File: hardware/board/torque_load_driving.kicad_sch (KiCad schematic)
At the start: 22 parts, among them J4 Conn_01x02_Female, Q1 IRF8707TRPBF, U1 ADS7049, U10 AD8615, U11 INA180A4, U12 UCC27537

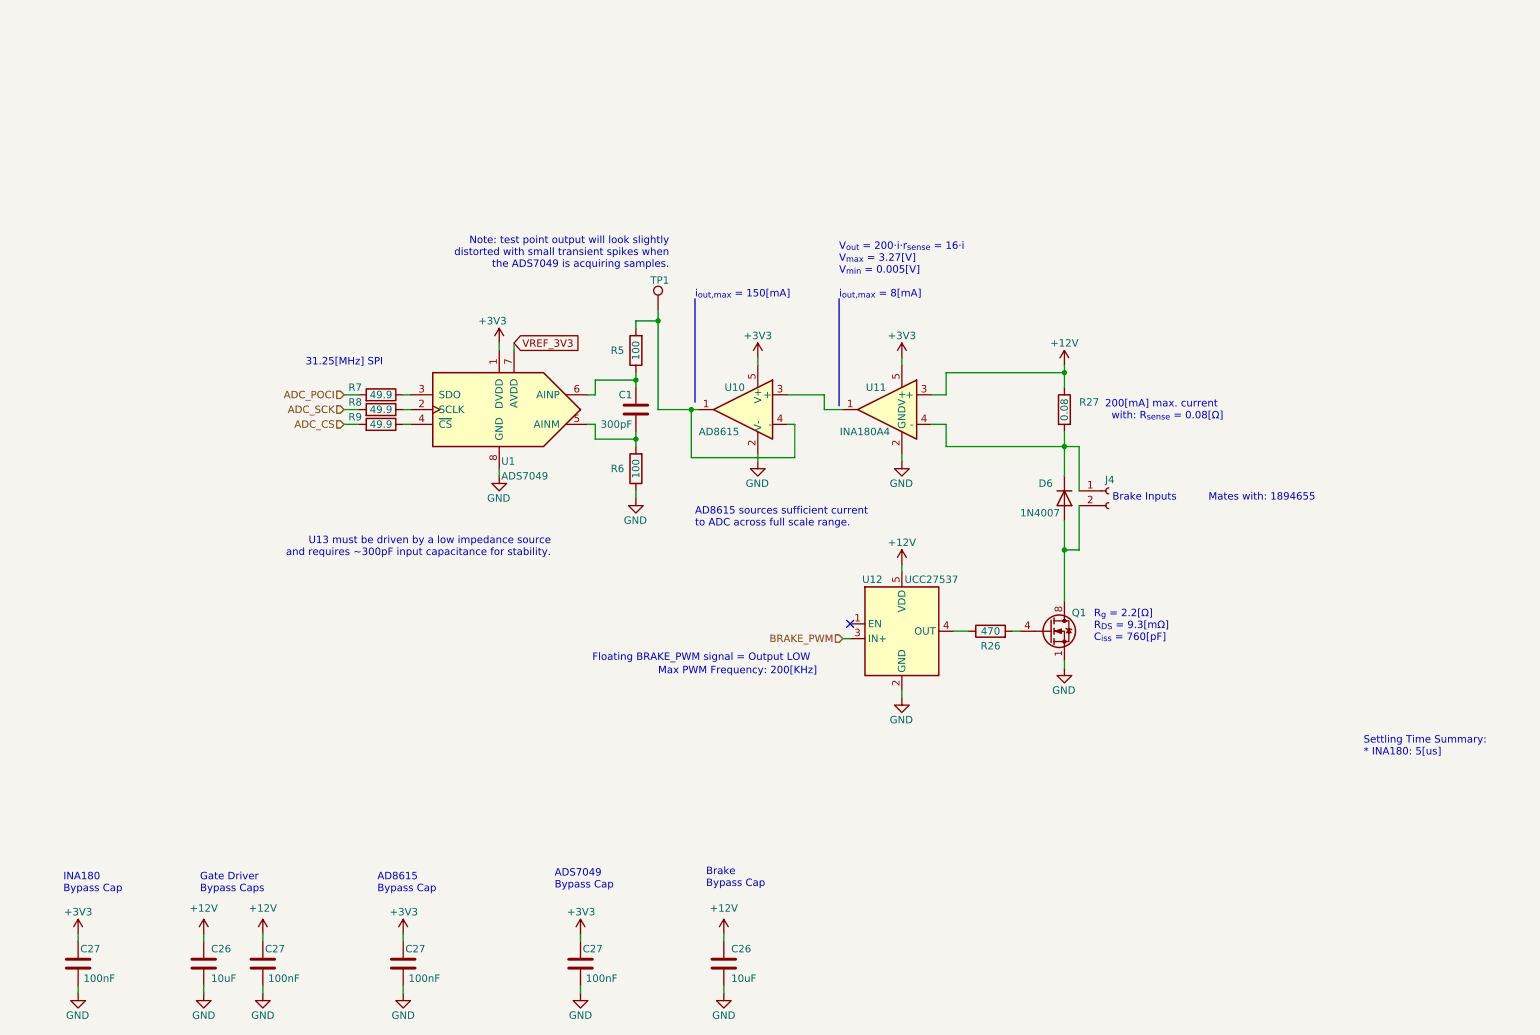
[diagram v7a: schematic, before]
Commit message: draft layout with analog brake driver circuit
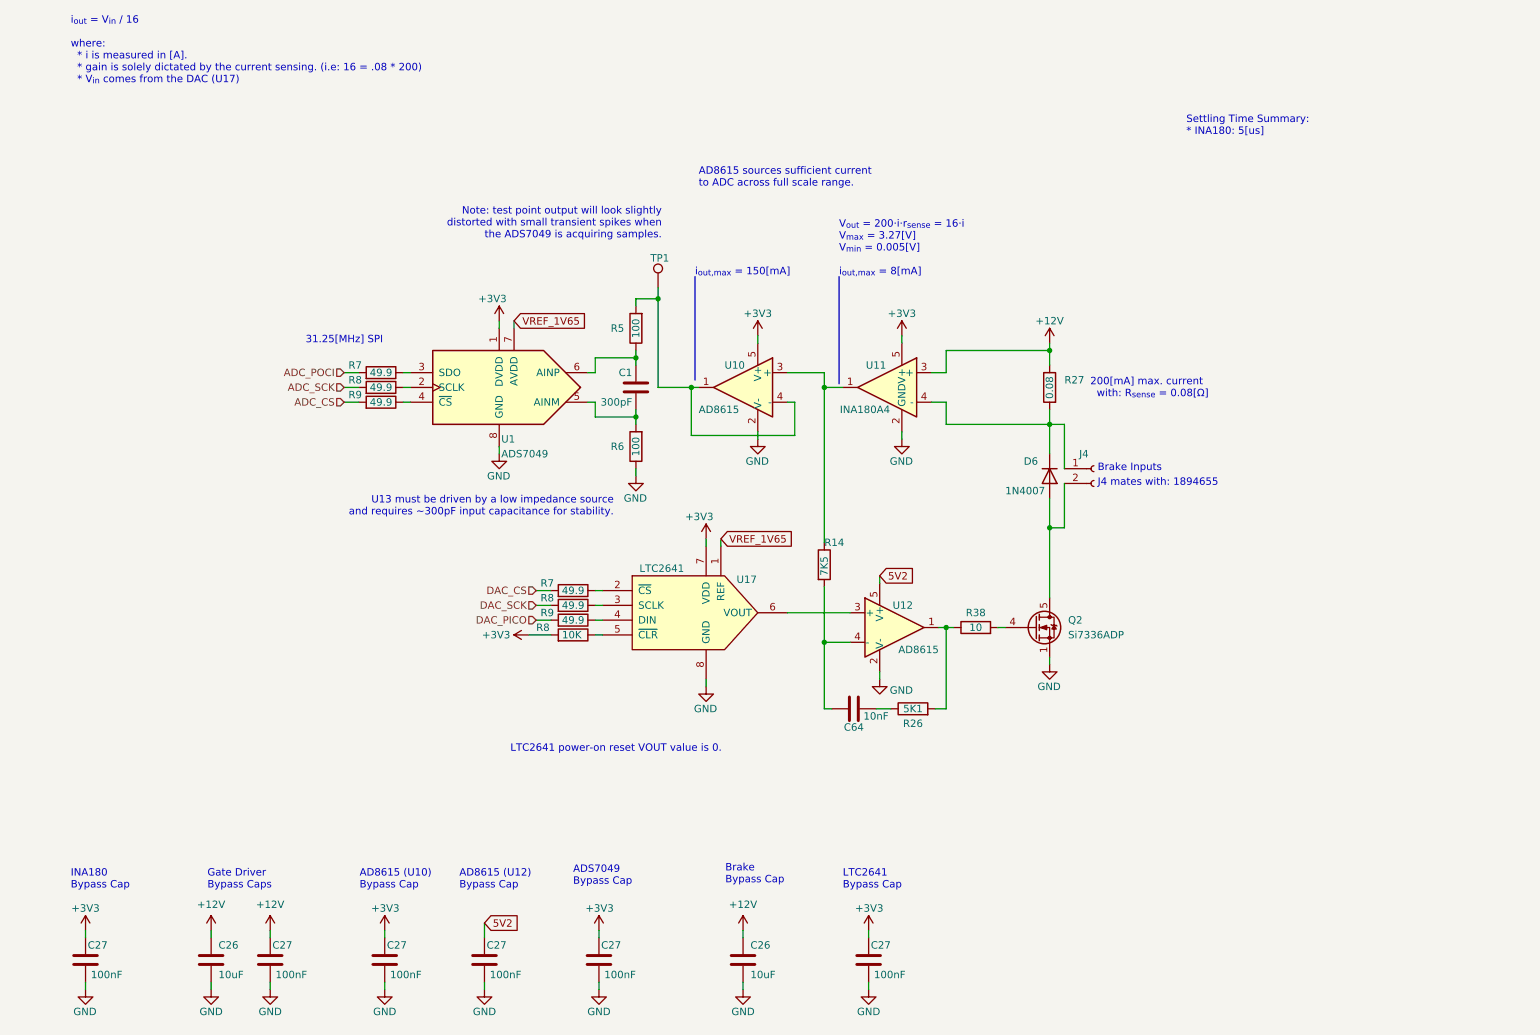
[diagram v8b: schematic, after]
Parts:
- removed Q1: IRF8707TRPBF, Package_SO:SOIC-8_3.9x4.9mm_P1.27mm, symbol Transistor_FET:IRF7403
- removed U12: UCC27537, Package_TO_SOT_SMD:SOT-23-5, symbol kicad_component_library:UCC27537
- added C27 (x2): 100nF, Capacitor_SMD:C_0402_1005Metric, symbol Device:C
- added C64: 10nF, Capacitor_SMD:C_0603_1608Metric, symbol Device:C
- added Q2: Si7336ADP, Package_SO:PowerPAK_SO-8_Single, symbol Transistor_FET:Si7336ADP
- added R14: 7K5, Resistor_SMD:R_0402_1005Metric, symbol Device:R
- added R38: 10, Resistor_SMD:R_0402_1005Metric, symbol Device:R
- added R7, R8, R9: 49.9, Resistor_SMD:R_0402_1005Metric, symbol Device:R
- added R8: 10K, Resistor_SMD:R_0402_1005Metric, symbol Device:R
- added U12: AD8615, Package_TO_SOT_SMD:TSOT-23-5, symbol kicad_component_library:AD8615
- added U17: LTC2641, Package_SO:MSOP-8_3x3mm_P0.65mm, symbol kicad_component_library:LTC2641
- R26: value 470 -> 5K1; footprint Resistor_SMD:R_0805_2012Metric -> Resistor_SMD:R_0402_1005Metric; Link https://www.digikey.com/en/products/detail/koa-speer-electr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 -> https://www.digikey.com/en/products/detail/yageo/RT0402BRD0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; Manufacturer Panasonic Electronic Components -> Yageo; Manufacturer Number SG73P2ATTD4700F -> RT0402BRD075K1L; Power 1/2W -> (none); Tolerance 1% -> 0.1%
- U11: Link (none) -> https://www.digikey.com/en/products/detail/texas-instrument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
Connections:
- net +3V3: now also C27.2, R8.2, U17.7 (VDD)
- net GND: now also C27.1, C27.1, Q2.1 (S), Q2.2 (S), Q2.3 (S), U12.2 (V-), U17.8 (GND), U17.9 (GND)
- net at D6.2 (A), J4.2 (Pin_2): now also Q2.5 (D)
- net at U10.3 (+), U11.1: now also R14.1
- net at R26.1: now also C64.2
- net at R26.2: now also R38.1, U12.1
- net VREF_3V3 renamed VREF_1V65
- net VREF_1V65: now also U17.1 (REF)
- new net: R9.1, U17.4 (DIN)
- new net: R8.1, U17.5 (~{CLR})
- new net: U12.3 (+), U17.6 (VOUT)
- new net: C64.1, R14.2, U12.4 (-)
- new net: R7.1, U17.2 (~{CS})
- new net: R8.1, U17.3 (SCLK)
- new net: Q2.4 (G), R38.2
- new net 5V2: C27.2, U12.5 (V+)
- new net DAC_CS: R7.2
- new net DAC_PICO: R9.2
- new net DAC_SCK: R8.2
- no-connect marks 1 -> 0
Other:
- note added: "AD8615 (U10) Bypass Cap"
- note added: "AD8615 (U12) Bypass Cap"
- note added: "J4 mates with: 1894655"
- note added: "LTC2641 Bypass Cap"
- note added: "LTC2641 power-on reset VOUT value is 0."
- note added: "i_{out} = V_{in} / 16 where: * i is measured in [A]. * gain is solely dictated by the current sensing. (i.e: 16 = .08 * 200) * V_{in} comes from the DAC (U17)"
- note removed: "AD8615 Bypass Cap"
- note removed: "Floating BRAKE_PWM signal = Output LOW"
- note removed: "Mates with: 1894655"
- note removed: "Max PWM Frequency: 200[KHz]"
- note removed: "R_{g} = 2.2[Ω] R_{DS} = 9.3[mΩ] C_{iss} = 760[pF]"
- moved on the sheet: C1, C26, C27, D6, J4, R27, R5, R6, R7, R8, R9, TP1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
